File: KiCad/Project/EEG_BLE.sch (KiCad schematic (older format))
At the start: 17 parts, among them P1 ELECTRODES, U1 ADS1299, U2 NRF51822

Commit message: Schematics cosmetics
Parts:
- C1: value 1nF -> 10nF
- R1: value 1M -> 392k
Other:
- note added: "Where does \nVREFP connect to?"
- note removed: "Where does VREFP go?"
- moved on the sheet: BATTERY
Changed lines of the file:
@@
 P 2450 1650
 F 0 "R1" V 2530 1650 50  0000 C CNN
-F 1 "1M" V 2450 1650 50  0000 C CNN
+F 1 "392k" V 2450 1650 50  0000 C CNN
 F 2 "" V 2380 1650 50  0000 C CNN
 F 3 "" H 2450 1650 50  0000 C CNN
@@
 P 2450 1900
 F 0 "C1" H 2475 2000 50  0000 L CNN
-F 1 "1nF" H 2475 1800 50  0000 L CNN
+F 1 "10nF" H 2475 1800 50  0000 L CNN
 F 2 "" H 2488 1750 50  0000 C CNN
 F 3 "" H 2450 1900 50  0000 C CNN
@@
 Text GLabel 3150 4950 0    60   Input ~ 0
 VREFP
+Text Notes 2200 5100 0    60   ~ 0
+Where does \nVREFP connect to?
+Text Notes 2250 4300 0    43   ~ 0
+Do SRB1 and SRB2 \nneed to be connected \nto something \n(in this bias drive setup)?
+Text Notes 1450 3300 0    39   ~ 0
+Do I need \nRC circuits\non electrodes?
+Text Notes 3000 2600 0    31   ~ 0
+Do I need to connect \nBIASINV to something?
+Text Notes 2900 1600 0    39   ~ 0
+Do BIASOUT and BIASIN \nneed to be connected \nand why?
+Text Notes 2000 1550 0    47   ~ 0
+What is the optimum \nresistor value \nfor this bias drive?
+Text Notes 6000 1000 0    59   ~ 0
+3.3v (regulated)
+Text Notes 2500 850  0    59   ~ 0
+5V (regulated)
+$Comp
+L Battery BATTERY
+U 1 1 57DE7944
+P 5600 4850
+F 0 "BATTERY" H 5700 4900 50  0000 L CNN
+F 1 "5V" H 5700 4800 50  0000 L CNN
+F 2 "" V 5600 4890 50  0000 C CNN
+F 3 "" V 5600 4890 50  0000 C CNN
+	1    5600 4850
+	1    0    0    -1
+$EndComp
+$Comp
+L ADS1299 U1
+U 1 1 57D3263D
+P 3800 2950
+F 0 "U1" H 3800 2750 60  0000 C CNN
+F 1 "ADS1299" H 3800 3150 60  0000 C CNN
+F 2 "" H 3800 2950 60  0001 C CNN
+F 3 "" H 3800 2950 60  0001 C CNN
+	1    3800 2950
+	1    0    0    -1
+$EndComp
+Text Notes 3700 2600 0    31   ~ 0
+Do I need BIASREf?\nAdvantages over internal?
+Text Notes 2500 950  0    39   ~ 0
+Is unipolar or bipolar better?
+Text Notes 6000 1250 0    43   ~ 0
+Can it share ground \nwith analog supply \n(connected DGND and VSS)?
+Text Notes 1400 1700 0    43   ~ 0
+Is capacitor \n(RC circuit)\nneeded here? \nHow to choose its value?
+Text Notes 1450 3550 0    39   ~ 0
+If YES, \nhow to choose \nRC values?
+Text Notes 4600 4650 0    43   ~ 0
+Enought capacitors?\nWould ground and supply \nplanes be better instead?
+Text Notes 4250 1000 0    43   ~ 0
+Enought capacitros?\nWould ground and supply \nplanes be better instead?
+$Comp
+L LP2987AIMM-5.0/NOPB U?
+U 1 1 57DE8D4A
+P 7200 4750
+F 0 "U?" H 6900 5050 50  0000 C CNN
+F 1 "LP2987AIMM-5.0/NOPB" H 7400 5050 50  0000 C CNN
+F 2 "MSOP-8" H 7200 4750 50  0000 C CIN
+F 3 "" H 7200 4750 50  0000 C CNN
+	1    7200 4750
+	1    0    0    -1
+$EndComp
+$Comp
+L C C?
+U 1 1 57DE8FE2
+P 7950 4950
+F 0 "C?" H 7975 5050 50  0000 L CNN
+F 1 "C" H 7975 4850 50  0000 L CNN
+F 2 "" H 7988 4800 50  0000 C CNN
+F 3 "" H 7950 4950 50  0000 C CNN
+	1    7950 4950
+	1    0    0    -1
+$EndComp
+$Comp
+L C C?
+U 1 1 57DE91C6
+P 6450 4900
+F 0 "C?" H 6475 5000 50  0000 L CNN
+F 1 "C" H 6475 4800 50  0000 L CNN
+F 2 "" H 6488 4750 50  0000 C CNN
+F 3 "" H 6450 4900 50  0000 C CNN
+	1    6450 4900
+	1    0    0    -1
+$EndComp
+Text GLabel 8250 4700 2    39   Input ~ 0
+AVDD
+Text GLabel 8250 5150 2    39   Input ~ 0
+AVSS
+$Comp
+L LP2987IMMX-3.3/NOPB U?
+U 1 1 57DE9BCA
+P 7200 5600
+F 0 "U?" H 6900 5900 50  0000 C CNN
+F 1 "LP2987IMMX-3.3/NOPB" H 7400 5900 50  0000 C CNN
+F 2 "MSOP-8" H 7200 5600 50  0000 C CIN
+F 3 "" H 7200 5600 50  0000 C CNN
+	1    7200 5600
+	1    0    0    -1
+$EndComp
+$Comp
+L C C?
+U 1 1 57DE9DA6
+P 6450 5700
+F 0 "C?" H 6475 5800 50  0000 L CNN
+F 1 "C" H 6475 5600 50  0000 L CNN
+F 2 "" H 6488 5550 50  0000 C CNN
+F 3 "" H 6450 5700 50  0000 C CNN
+	1    6450 5700
+	1    0    0    -1
+$EndComp
+$Comp
+L C C?
+U 1 1 57DE9DFA
+P 7950 5700
+F 0 "C?" H 7975 5800 50  0000 L CNN
+F 1 "C" H 7975 5600 50  0000 L CNN
+F 2 "" H 7988 5550 50  0000 C CNN
+F 3 "" H 7950 5700 50  0000 C CNN
+	1    7950 5700
+	1    0    0    -1
+$EndComp
+Text GLabel 8300 5550 2    39   Input ~ 0
+VDD
+Text GLabel 8300 5950 2    39   Input ~ 0
+DGND
 Connection ~ 7750 4300
 Wire Wire Line
@@
 Wire Wire Line
 	4150 4450 4150 4150
-Text Notes 1750 5000 0    60   ~ 0
-Where does VREFP go?
-Text Notes 2300 4300 0    39   ~ 0
-Do SRB1 and SRB2 \nneed to be connected \nto something \n(in this bias drive setup)?
-Text Notes 1450 3300 0    35   ~ 0
-Do I need \nRC circuits\non electrodes?
-Text Notes 3000 2600 0    31   ~ 0
-Do I need to connect \nBIASINV to something?
-Text Notes 2850 1650 0    39   ~ 0
-Do BIASOUT and BIASIN \nneed to be connected \nand why?
-Text Notes 2000 1550 0    39   ~ 0
-What is the optimum \nresistor value \nfor this bias drive?
 Wire Notes Line
 	2200 1550 2300 1600
-Text Notes 6000 1000 0    59   ~ 0
-3.3v (regulated)
-Text Notes 2500 850  0    59   ~ 0
-5V (regulated)
-$Comp
-L Battery BATTERY
-U 1 1 57DE7944
-P 5900 4700
-F 0 "BATTERY" H 6000 4750 50  0000 L CNN
-F 1 "5V" H 6000 4650 50  0000 L CNN
-F 2 "" V 5900 4740 50  0000 C CNN
-F 3 "" V 5900 4740 50  0000 C CNN
-	1    5900 4700
-	1    0    0    -1
-$EndComp
-$Comp
-L ADS1299 U1
-U 1 1 57D3263D
-P 3800 2950
-F 0 "U1" H 3800 2750 60  0000 C CNN
-F 1 "ADS1299" H 3800 3150 60  0000 C CNN
-F 2 "" H 3800 2950 60  0001 C CNN
-F 3 "" H 3800 2950 60  0001 C CNN
-	1    3800 2950
-	1    0    0    -1
-$EndComp
-Text Notes 3700 2600 0    31   ~ 0
-Do I need BIASREf?\nAdvantages over internal?
 Wire Notes Line
 	3800 2450 3500 2300
 Wire Notes Line
 	3200 2450 3300 2350
-Text Notes 2500 950  0    39   ~ 0
-Is unipolar or bipolar better?
 Wire Notes Line
 	2450 750  2450 1000
@@
 	3400 1000 3400 750
 Wire Notes Line
-	3400 750  2450 750
-Wire Notes Line
 	2450 800  2450 850
-Text Notes 6000 1250 0    39   ~ 0
-Can it share ground \nwith analog supply \n(connected DGND and VSS)?
 Wire Notes Line
 	5950 850  5950 1300
@@
 Wire Notes Line
 	6900 850  5950 850
-Text Notes 1750 2000 0    28   ~ 0
-Is capacitor \n(RC circuit)\nneeded here? \nHow to choose its value?
-Wire Notes Line
-	2050 2000 2050 2050
-Wire Notes Line
-	2050 2050 2450 2050
-Wire Notes Line
-	2450 2050 2450 1900
-Text Notes 1450 3550 0    39   ~ 0
-If YES, \nhow to choose \nRC values?
-Text Notes 4550 4600 0    39   ~ 0
-Enought capacitors?\nWould ground and supply \nplanes be better instead?
-Text Notes 4250 1000 0    39   ~ 0
-Enought capacitros?\nWould ground and supply \nplanes be better instead?
-Wire Wire Line
-	5900 4550 6700 4550
-$Comp
-L LP2987AIMM-5.0/NOPB U?
-U 1 1 57DE8D4A
-P 7200 4750
-F 0 "U?" H 6900 5050 50  0000 C CNN
-F 1 "LP2987AIMM-5.0/NOPB" H 7400 5050 50  0000 C CNN
-F 2 "MSOP-8" H 7200 4750 50  0000 C CIN
-F 3 "" H 7200 4750 50  0000 C CNN
-	1    7200 4750
-	1    0    0    -1
-$EndComp
-Wire Wire Line
-	5900 4850 5900 5950
-Wire Wire Line
-	5900 5150 8250 5150
+Wire Wire Line
+	5600 4550 6700 4550
+Wire Wire Line
+	5600 5150 8250 5150
 Wire Wire Line
 	7200 5150 7200 5100
@@
 Wire Wire Line
 	7700 4700 8250 4700
-$Comp
-L C C?
-U 1 1 57DE8FE2
-P 7950 4950
-F 0 "C?" H 7975 5050 50  0000 L CNN
-F 1 "C" H 7975 4850 50  0000 L CNN
-F 2 "" H 7988 4800 50  0000 C CNN
-F 3 "" H 7950 4950 50  0000 C CNN
-	1    7950 4950
-	1    0    0    -1
-$EndComp
 Wire Wire Line
 	7950 4800 7950 4700
@@
 	7950 5100 7950 5150
 Connection ~ 7950 5150
-$Comp
-L C C?
-U 1 1 57DE91C6
-P 6450 4900
-F 0 "C?" H 6475 5000 50  0000 L CNN
-F 1 "C" H 6475 4800 50  0000 L CNN
-F 2 "" H 6488 4750 50  0000 C CNN
-F 3 "" H 6450 4900 50  0000 C CNN
-	1    6450 4900
-	1    0    0    -1
-$EndComp
 Wire Wire Line
 	6450 4550 6450 4750
@@
 	6450 5050 6450 5150
 Connection ~ 6450 5150
-Text GLabel 8250 4700 2    39   Input ~ 0
-AVDD
-Text GLabel 8250 5150 2    39   Input ~ 0
-AVSS
-$Comp
-L LP2987IMMX-3.3/NOPB U?
-U 1 1 57DE9BCA
-P 7200 5600
-F 0 "U?" H 6900 5900 50  0000 C CNN
-F 1 "LP2987IMMX-3.3/NOPB" H 7400 5900 50  0000 C CNN
-F 2 "MSOP-8" H 7200 5600 50  0000 C CIN
-F 3 "" H 7200 5600 50  0000 C CNN
-	1    7200 5600
-	1    0    0    -1
-$EndComp
-Connection ~ 5900 5150
 Wire Wire Line
 	6300 4550 6300 5400
@@
 	6300 5400 6700 5400
 Connection ~ 6300 4550
-$Comp
-L C C?
-U 1 1 57DE9DA6
-P 6450 5700
-F 0 "C?" H 6475 5800 50  0000 L CNN
-F 1 "C" H 6475 5600 50  0000 L CNN
-F 2 "" H 6488 5550 50  0000 C CNN
-F 3 "" H 6450 5700 50  0000 C CNN
-	1    6450 5700
-	1    0    0    -1
-$EndComp
-$Comp
-L C C?
-U 1 1 57DE9DFA
-P 7950 5700
-F 0 "C?" H 7975 5800 50  0000 L CNN
-F 1 "C" H 7975 5600 50  0000 L CNN
-F 2 "" H 7988 5550 50  0000 C CNN
-F 3 "" H 7950 5700 50  0000 C CNN
-	1    7950 5700
-	1    0    0    -1
-$EndComp
 Wire Wire Line
 	6450 5550 6450 5400
@@
 	7700 5550 8300 5550
 Wire Wire Line
-	5900 5950 8300 5950
+	5600 5950 8300 5950
 Wire Wire Line
 	7950 5850 7950 5950
 Connection ~ 7950 5950
 Connection ~ 7950 5550
-Text GLabel 8300 5550 2    39   Input ~ 0
-VDD
-Text GLabel 8300 5950 2    39   Input ~ 0
-DGND
+Wire Wire Line
+	5600 4550 5600 4700
+Wire Wire Line
+	5600 5000 5600 5950
+Connection ~ 5600 5150
+Wire Notes Line
+	3400 750  2450 750
+Wire Notes Line
+	2100 1700 2400 1850
 $EndSCHEMATC

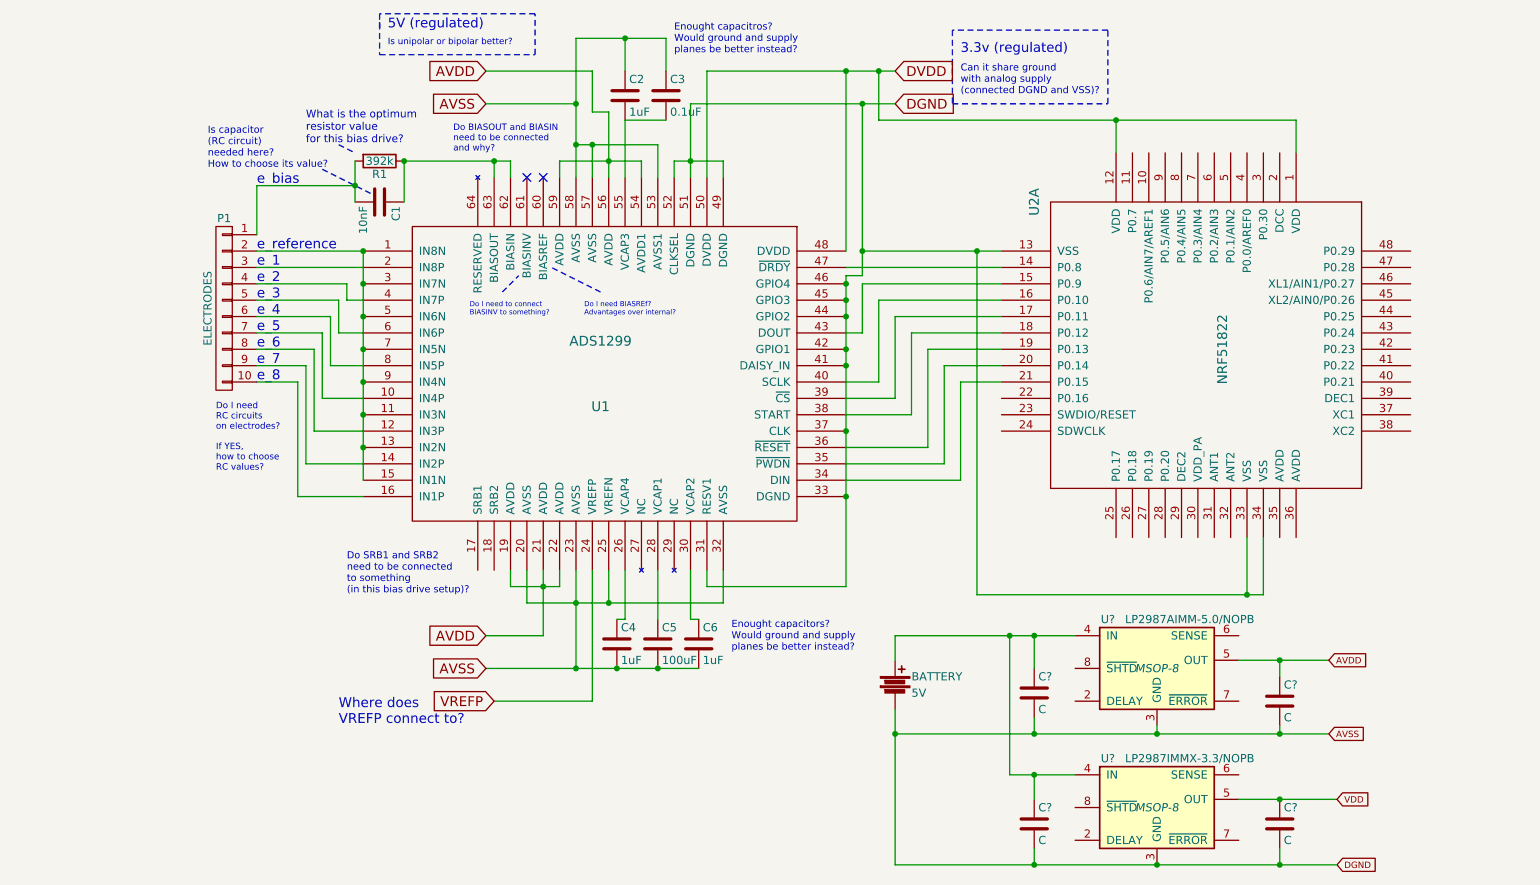
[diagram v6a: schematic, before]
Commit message: Using more popular voltage regulator for power supplies
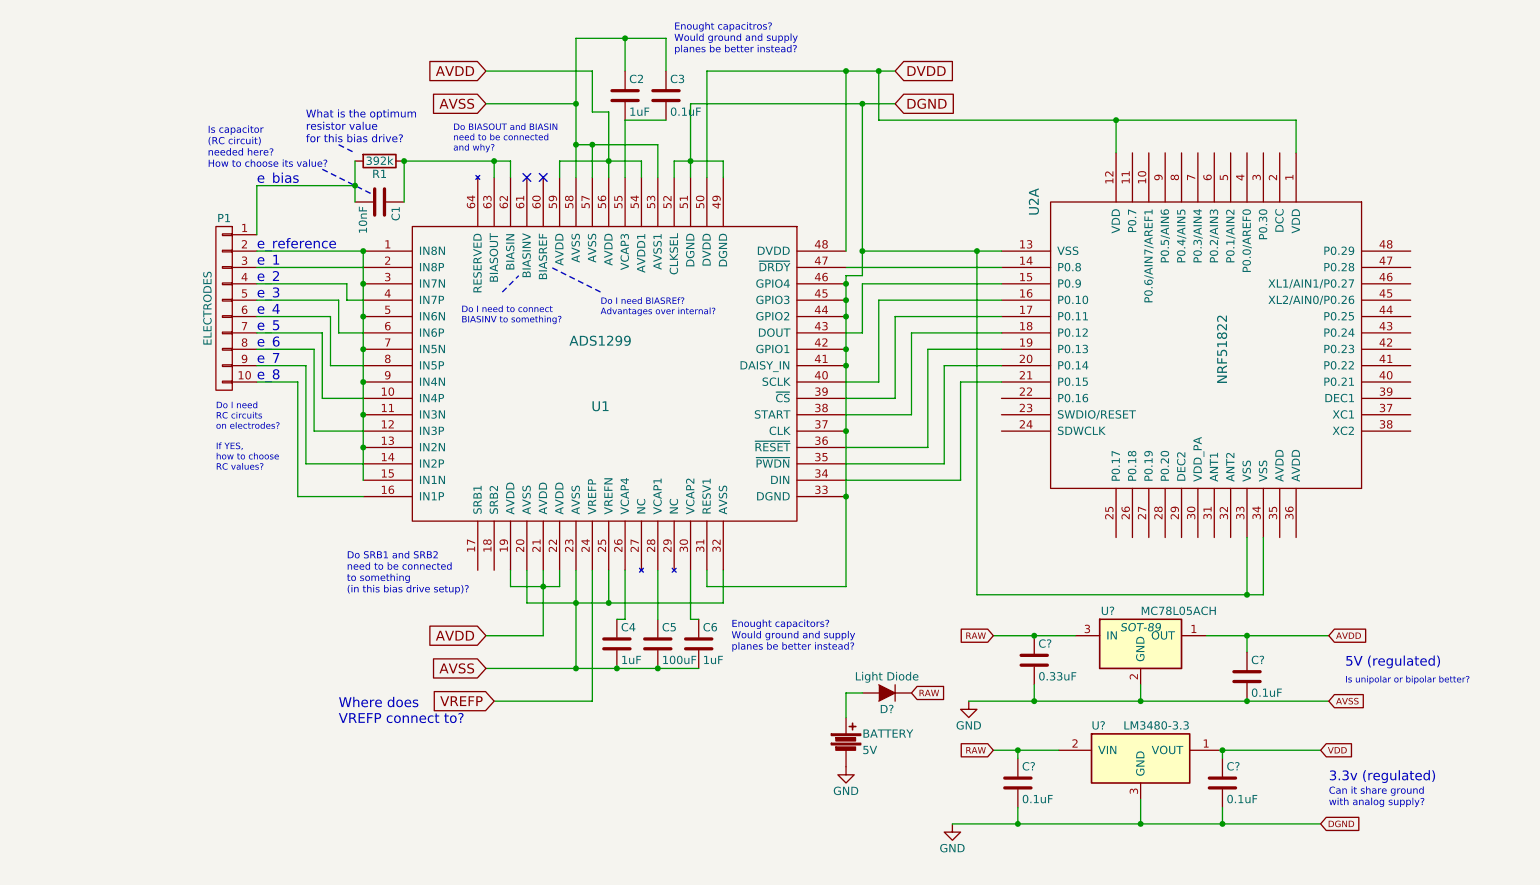
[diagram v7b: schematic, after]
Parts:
- removed U?: LP2987AIMM-5.0/NOPB, MSOP-8, symbol LP2987AIMM-5.0/NOPB
- removed U?: LP2987IMMX-3.3/NOPB, MSOP-8, symbol LP2987IMMX-3.3/NOPB
- added D?: Light Diode, symbol D
- added U?: MC78L05ACH, SOT-89, symbol MC78L05ACH
- added U?: LM3480-3.3, TO_SOT_Packages_SMD:SOT-23, symbol LM3480-3.3
- C? (x3): value C -> 0.1uF
- C?: value C -> 0.33uF
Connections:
- net AVDD: now also U?.1 (OUT)
- net VDD: now also U?.1 (VOUT)
- net RAW: now reaches C?.1, C?.1
- net RAW: now also D?.1 (K), U?.2 (VIN), U?.3 (IN); no longer BATTERY.1
- net AVSS renamed GND
- net GND: now also U?.2 (GND), U?.3 (GND)
- new net: BATTERY.1, D?.2 (A)
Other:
- note added: "Can it share ground \nwith analog supply?"
- note removed: "Can it share ground \nwith analog supply \n(connected DGND and VSS)?"
- moved on the sheet: BATTERY, C?

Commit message: Removes obsolete connections and components
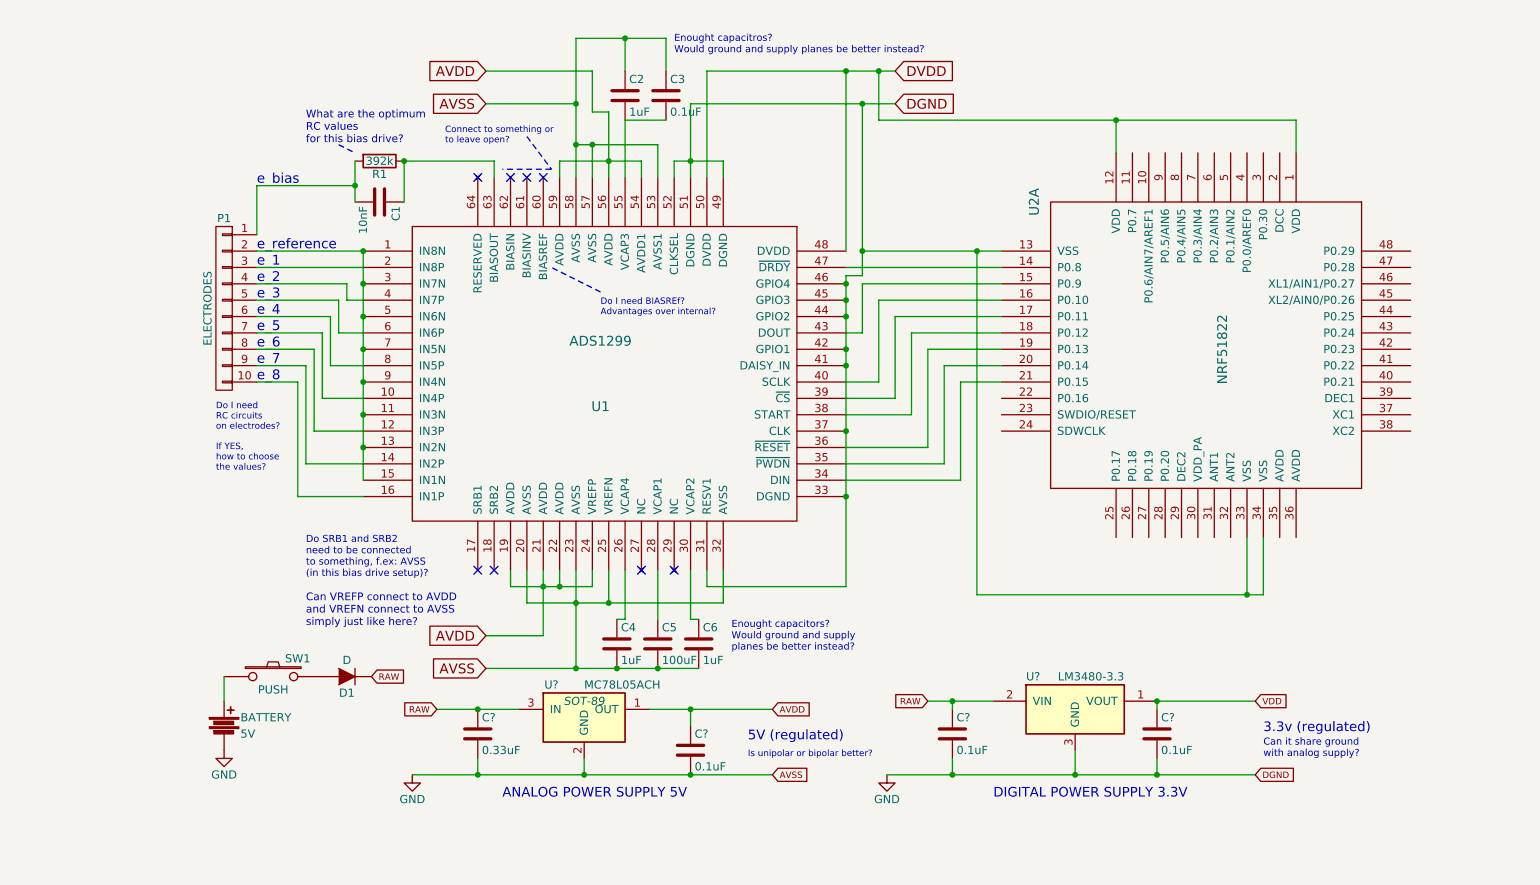
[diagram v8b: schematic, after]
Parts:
- added SW1: PUSH, symbol SW_PUSH
- D1: renamed from D?; value Light Diode -> D
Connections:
- net VREFP is gone; now on net AVDD: U1.24 (VREFP)
- net at C1.1, R1.1, U1.63 (BIASOUT): no longer U1.62 (BIASIN)
- net at BATTERY.1: now also SW1.1; no longer D1.2 (A)
- new net: D1.2 (A), SW1.2
- no-connect marks 2 -> 8
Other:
- note added: "ANALOG POWER SUPPLY 5V"
- note added: "Can VREFP connect to AVDD \nand VREFN connect to AVSS \nsimply just like here?"
- note added: "Connect to something or \nto leave open?"
- note added: "DIGITAL POWER SUPPLY 3.3V"
- note added: "Do SRB1 and SRB2 \nneed to be connected \nto something, f.ex: AVSS\n(in this bias drive setup)?"
- note added: "Enought capacitros?\nWould ground and supply planes be better instead?"
- note added: "If YES, \nhow to choose \nthe values?"
- note added: "What are the optimum \nRC values\nfor this bias drive?"
- note removed: "Do BIASOUT and BIASIN \nneed to be connected \nand why?"
- note removed: "Do I need to connect \nBIASINV to something?"
- note removed: "Do SRB1 and SRB2 \nneed to be connected \nto something \n(in this bias drive setup)?"
- note removed: "Enought capacitros?\nWould ground and supply \nplanes be better instead?"
- note removed: "If YES, \nhow to choose \nRC values?"
- note removed: "Is capacitor \n(RC circuit)\nneeded here? \nHow to choose its value?"
- note removed: "What is the optimum \nresistor value \nfor this bias drive?"
- note removed: "Where does \nVREFP connect to?"
- moved on the sheet: BATTERY, C?, D1, U?
